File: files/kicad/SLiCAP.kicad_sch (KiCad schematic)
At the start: 36 parts, among them K1 {k}, T1 0

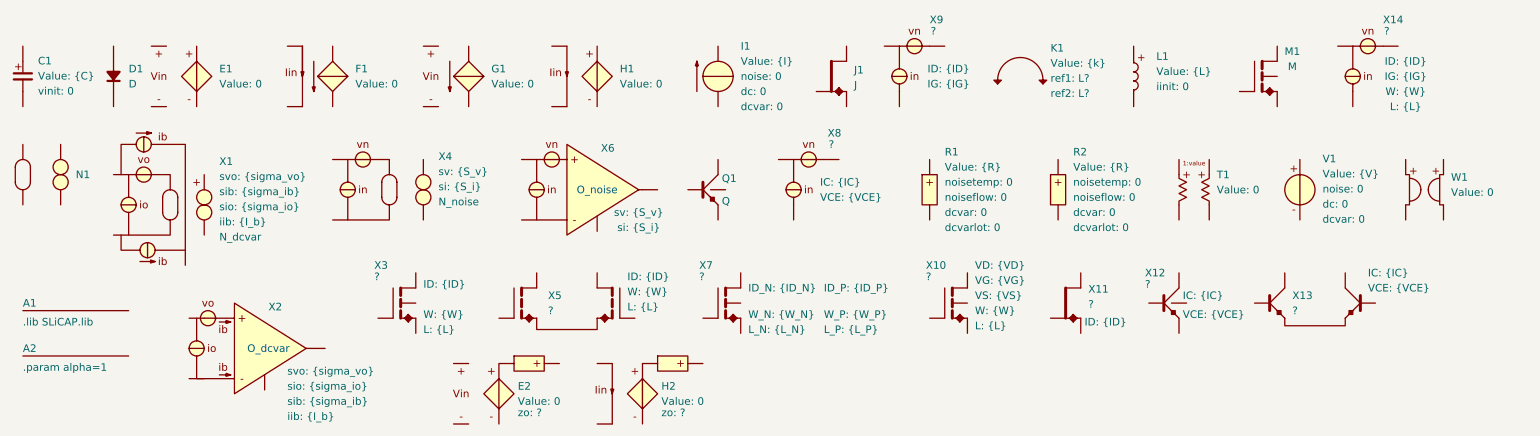
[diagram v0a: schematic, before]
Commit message: Updated KiCAD interface
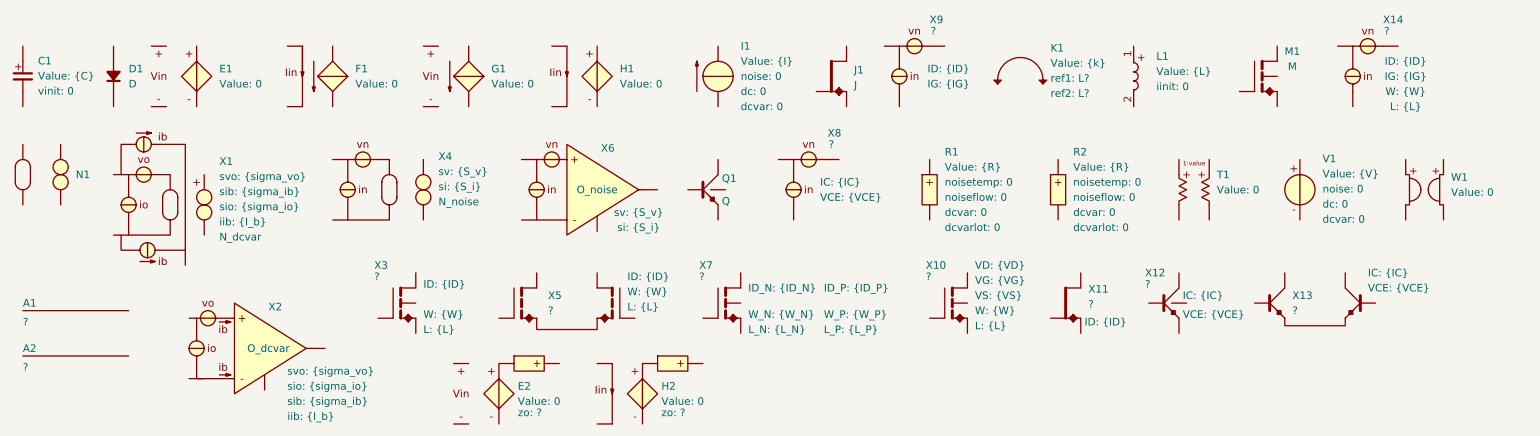
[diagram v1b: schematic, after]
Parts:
- A1: command .lib SLiCAP.lib -> ?
- A2: command .param alpha=1 -> ?

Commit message: Updated KiCAD interface
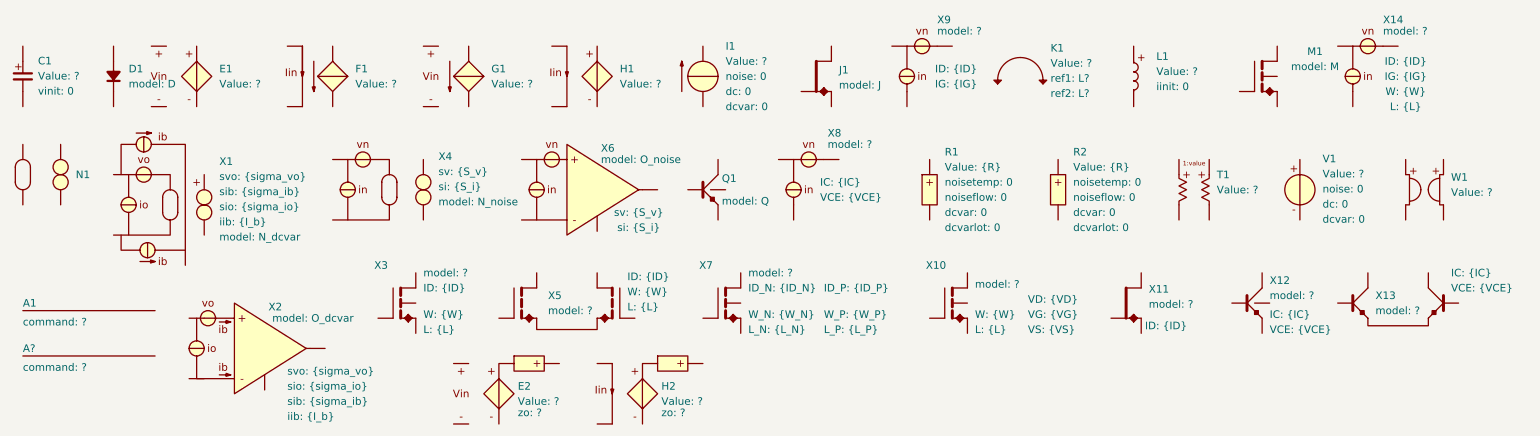
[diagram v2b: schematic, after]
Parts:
- A1, D1, J1, M1, N1, Q1, X1, X10, X11, X12, X13, X14, X2, X3, X4, X5, X6, X7, X8, X9: value ~ -> (none)
- A?: renamed from A2; value ~ -> (none)
- C1: value {C} -> ?
- E1, E2, F1, G1, H1, H2, T1, W1: value 0 -> ?
- I1: value {I} -> ?
- K1: value {k} -> ?
- L1: value {L} -> ?
- V1: value {V} -> ?
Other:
- moved on the sheet: A1, A?, I1, J1, X11, X12, X13, X9

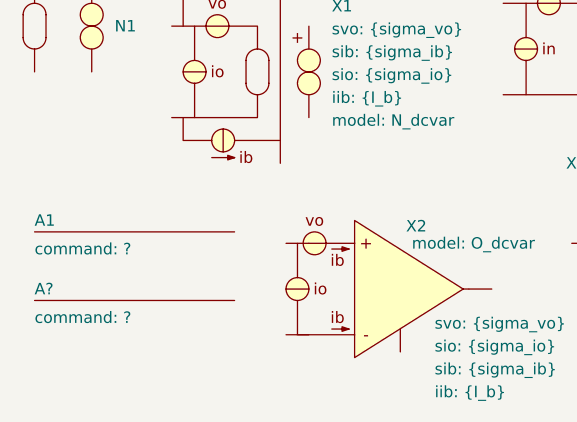
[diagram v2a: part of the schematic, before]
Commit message: Updated KiCAD interface
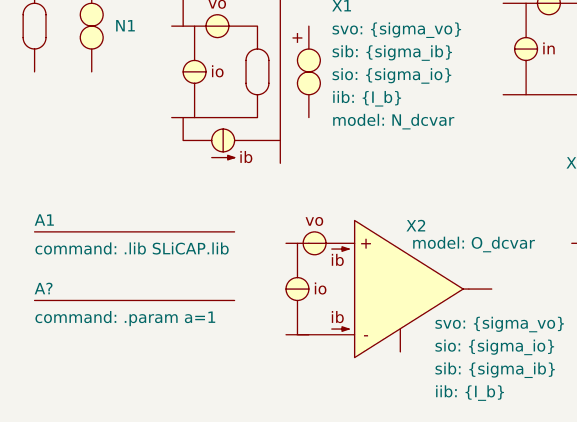
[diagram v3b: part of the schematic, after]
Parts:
- A1: value (none) -> ~; command ? -> .lib SLiCAP.lib
- A?: value (none) -> ~; command ? -> .param a=1
- D1, J1, M1, N1, Q1, X1, X10, X11, X12, X13, X14, X2, X3, X4, X5, X6, X7, X8, X9: value (none) -> ~

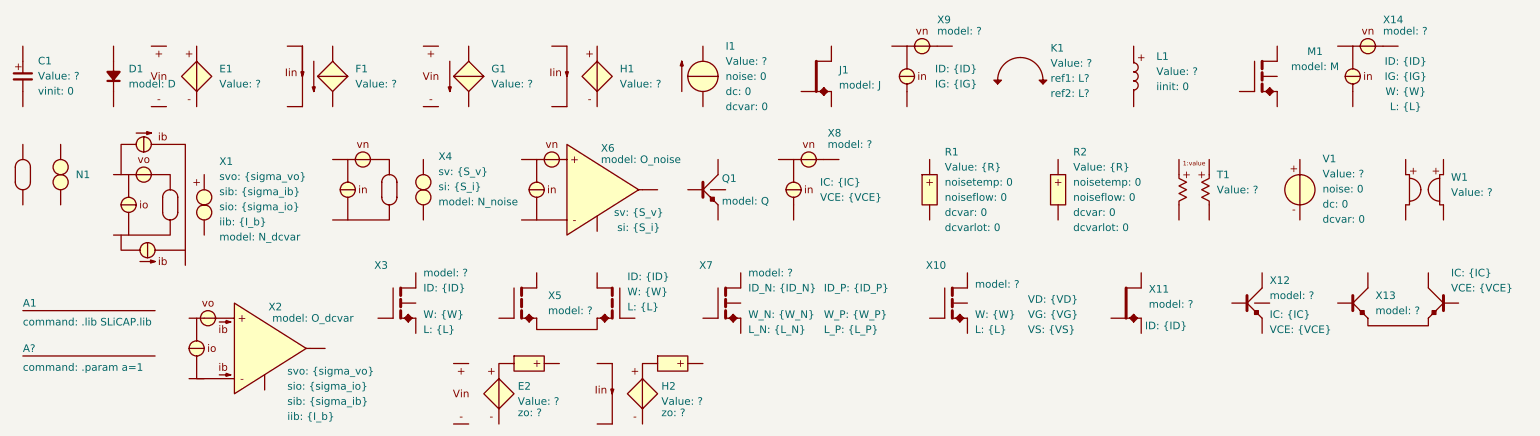
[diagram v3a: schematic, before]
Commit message: Fixed KiCad 8.0 compatibility
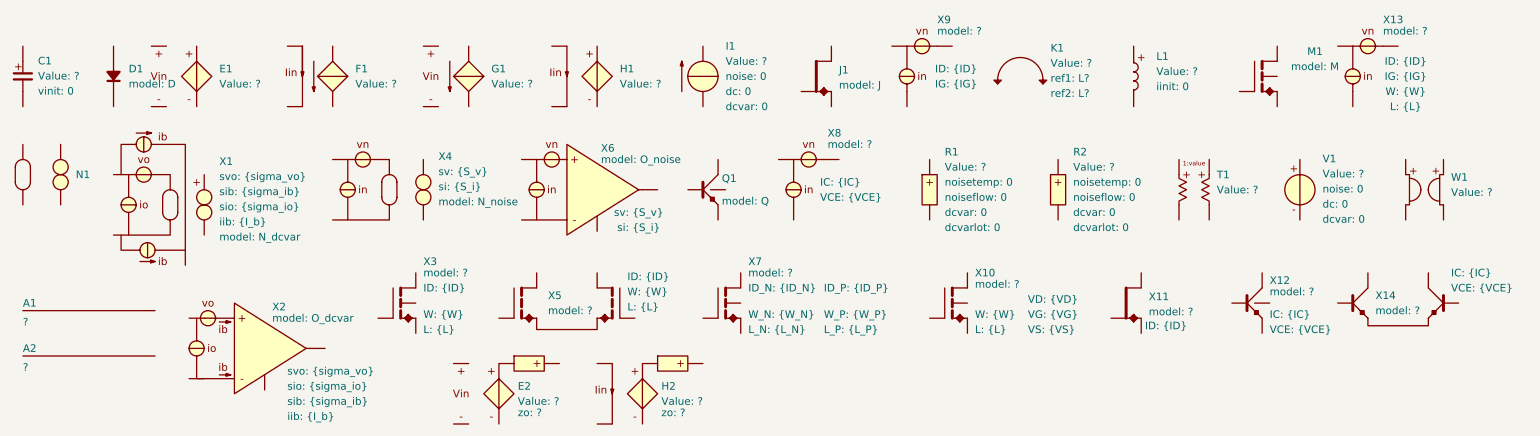
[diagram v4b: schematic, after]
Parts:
- A1: command .lib SLiCAP.lib -> ?
- A2: renamed from A?; command .param a=1 -> ?
- R1, R2: value {R} -> ?
- renumbered X14 to X13, X13 to X14
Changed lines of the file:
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@@
-(kicad_sch (version 20230121) (generator eeschema)
-  (paper "A4")
-  (title_block
-    (title "SLiCAP symbols")
-  )
+(kicad_sch
+	(version 20231120)
+	(generator "eeschema")
+	(generator_version "8.0")
+	(paper "A4")
+	(title_block
+		(title "SLiCAP symbols")
+	)

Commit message: Update kicad SLiCAP symbol library
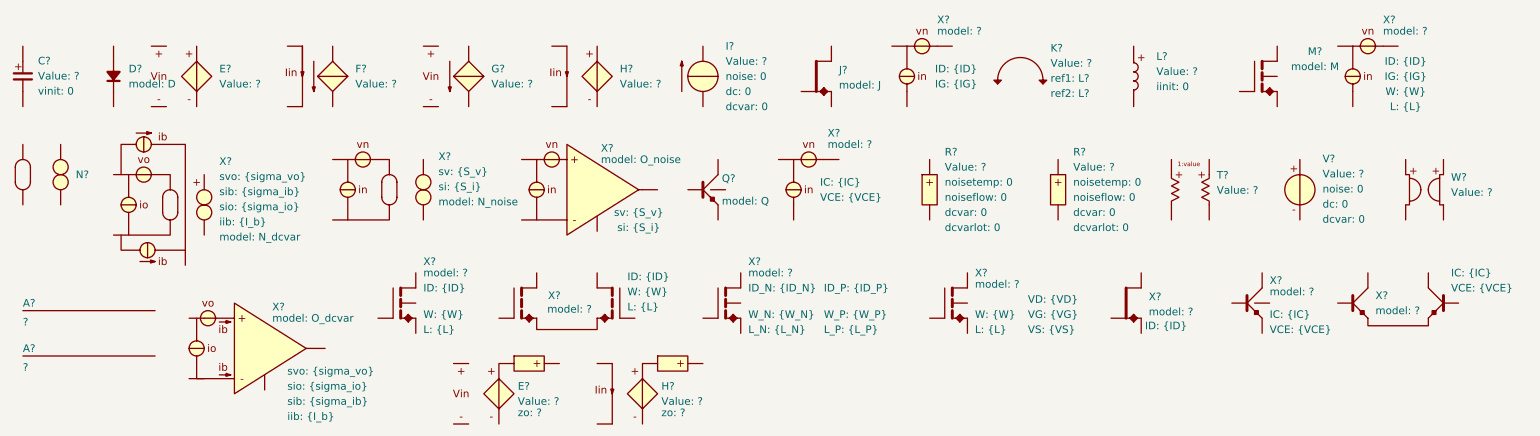
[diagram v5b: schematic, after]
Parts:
- A?: renamed from A1; value ~ -> (none)
- A?: renamed from A2; value ~ -> (none)
- D?: renamed from D1; value ~ -> (none)
- J?: renamed from J1; value ~ -> (none)
- M?: renamed from M1; value ~ -> (none)
- N?: renamed from N1; value ~ -> (none)
- Q?: renamed from Q1; value ~ -> (none)
- X?: renamed from X4; value ~ -> (none)
- X?: renamed from X11; value ~ -> (none)
- X?: renamed from X9; value ~ -> (none)
- X?: renamed from X14; value ~ -> (none)
- X?: renamed from X6; value ~ -> (none)
- X?: renamed from X5; value ~ -> (none)
- X?: renamed from X7; value ~ -> (none)
- X?: renamed from X12; value ~ -> (none)
- X?: renamed from X1; value ~ -> (none)
- X?: renamed from X10; value ~ -> (none)
- X?: renamed from X2; value ~ -> (none)
- X?: renamed from X8; value ~ -> (none)
- X?: renamed from X13; value ~ -> (none)
- X?: renamed from X3; value ~ -> (none)
- renumbered C1 to C?, E2 to E?, E1 to E?, F1 to F?, G1 to G?, H2 to H?, H1 to H?, I1 to I?, K1 to K?, L1 to L?, R1 to R?, R2 to R?, T1 to T?, V1 to V?, W1 to W?
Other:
- moved on the sheet: T?
